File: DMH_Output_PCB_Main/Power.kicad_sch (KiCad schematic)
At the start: 79 parts, among them J0 Conn_01x01, J10 Conn_01x06, J100 IDC_02x05, J23 Conn_01x06, U1 TL072, U10 NE5532, U11 TL074, U12 NE5532, U13 NE5532, U14 NE5532, U15 NE5532, U16 NE5532, U17 NE5532, U18 NE5532, U19 NE5532, U2 LM339, U20 TL072, U21 LM4040LP-10, U24 LM339, U25 LM339, U3 LM339, U4 LM339, U5 LM339, U6 LM339, U7 TL072, U8 TL074, U9 NE5532

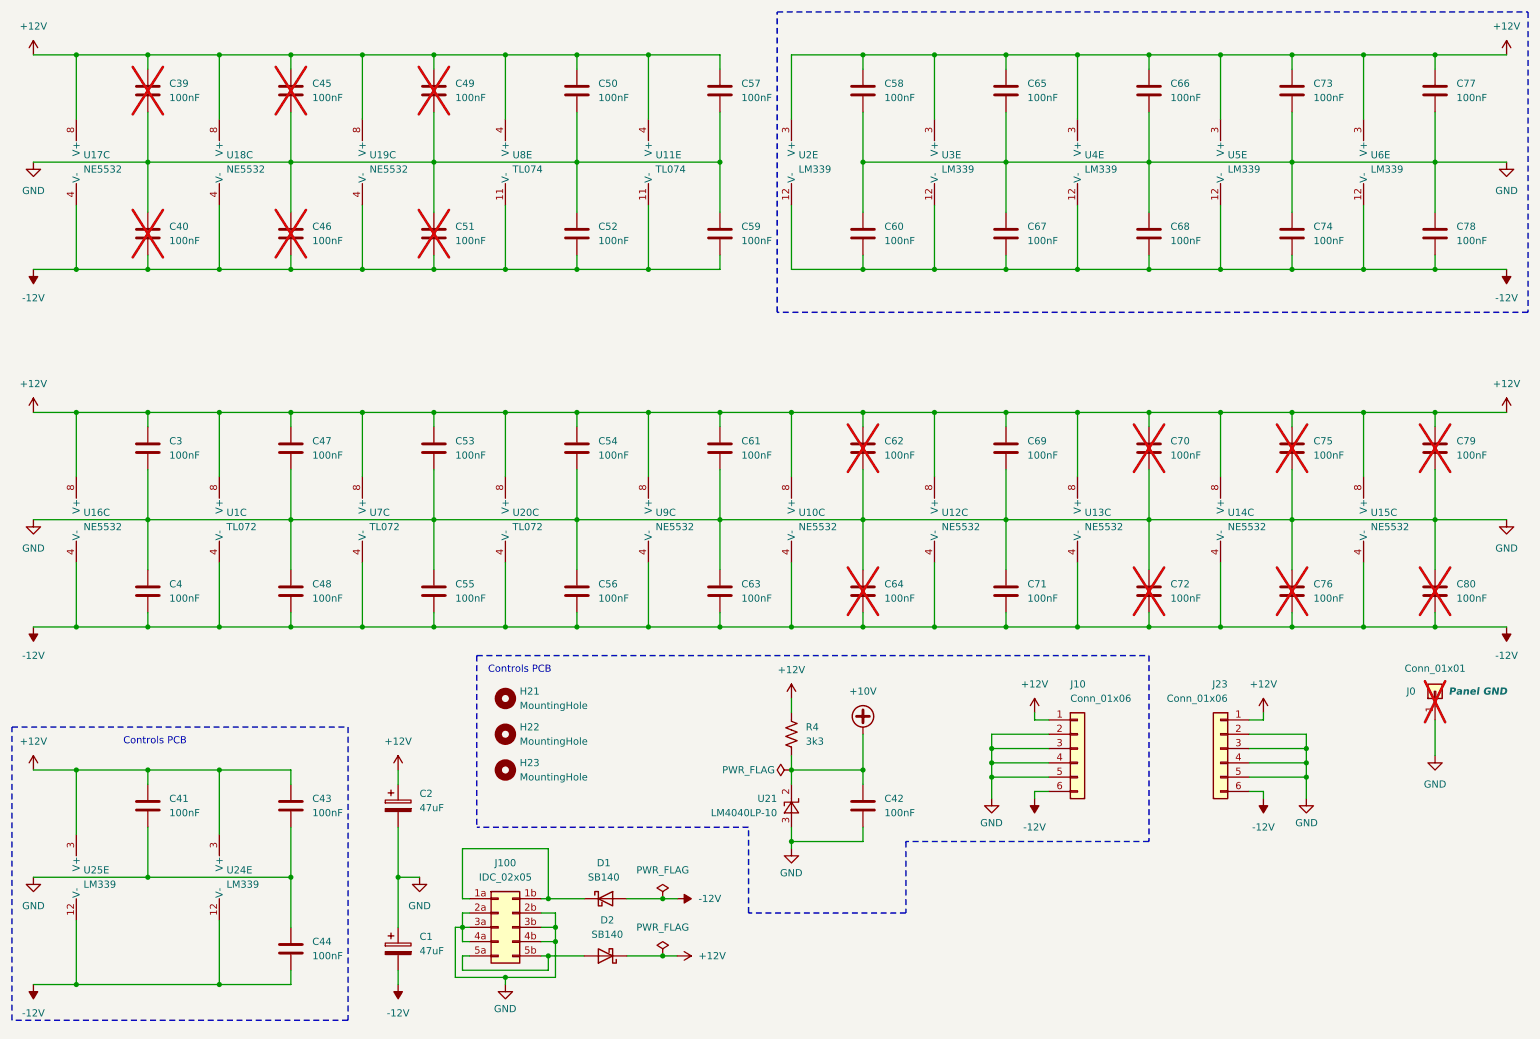
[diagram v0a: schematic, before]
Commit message: Preparing for split in submodules
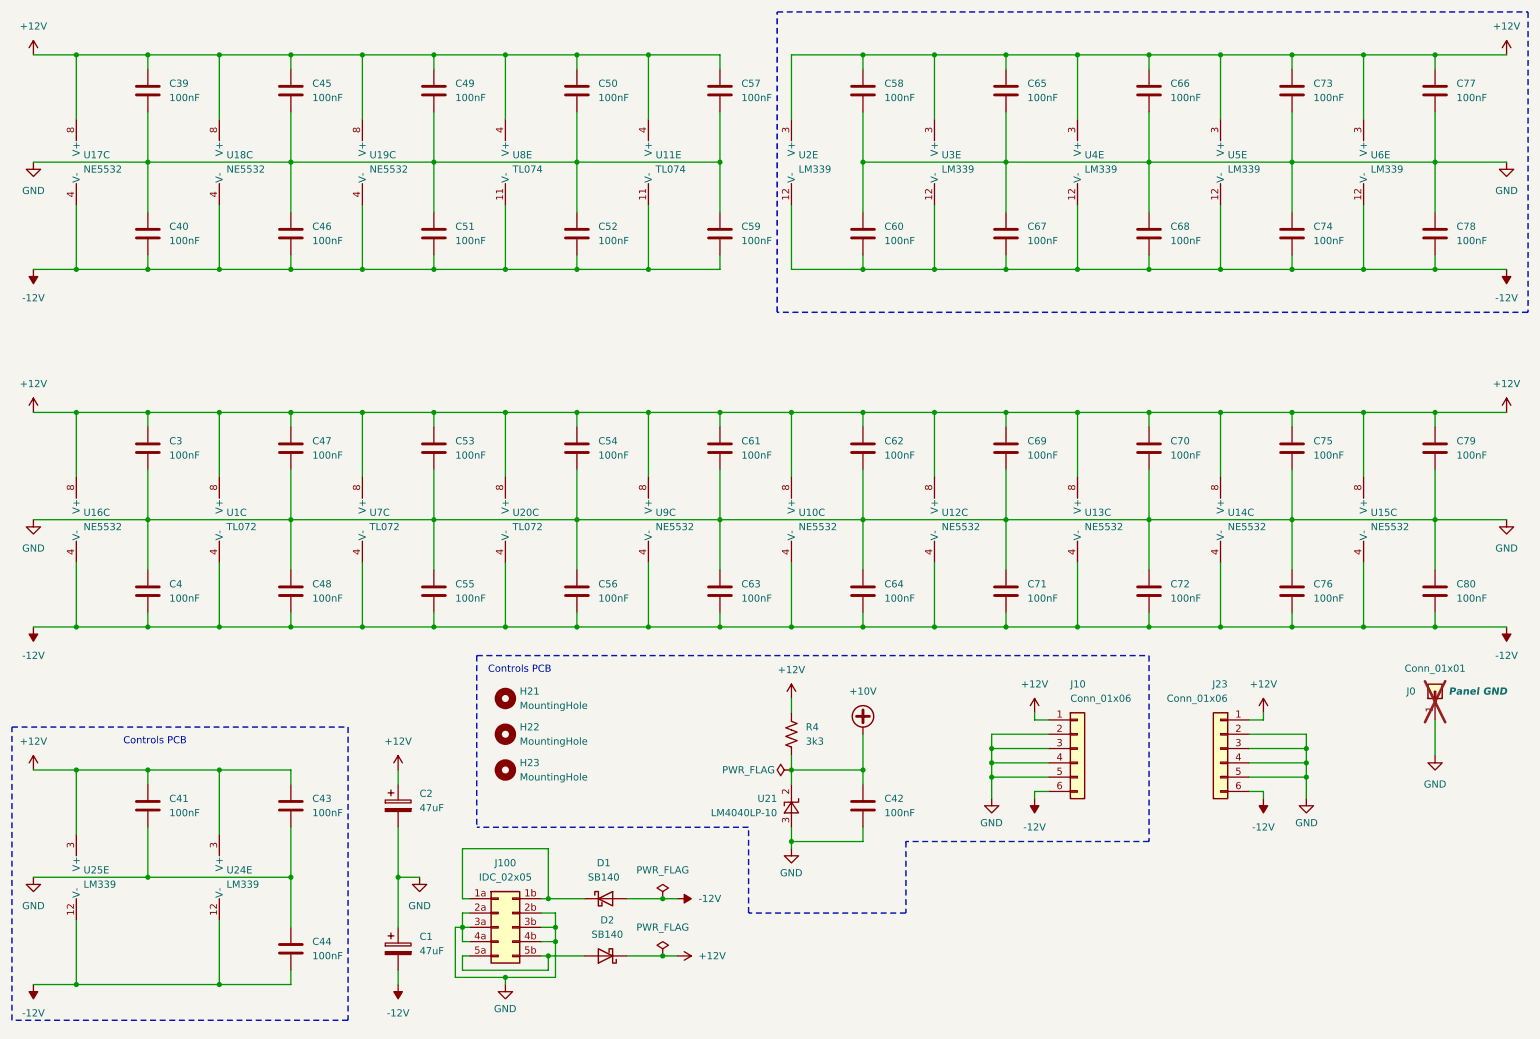
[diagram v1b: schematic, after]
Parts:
- C39, C40, C45, C46, C49, C51, C62, C64, C70, C72, C75, C76, C79, C80: now fitted; now in the parts list
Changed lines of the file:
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@@
 		(unit 1)
 		(exclude_from_sim no)
-		(in_bom no)
-		(on_board no)
-		(dnp yes)
+		(in_bom yes)
+		(on_board yes)
+		(dnp no)
 		(fields_autoplaced yes)
 		(property "Reference" "C76"
@@
 		(unit 1)
 		(exclude_from_sim no)
-		(in_bom no)
-		(on_board no)
-		(dnp yes)
+		(in_bom yes)
+		(on_board yes)
+		(dnp no)
 		(fields_autoplaced yes)
 		(property "Reference" "C75"
@@
 		(unit 1)
 		(exclude_from_sim no)
-		(in_bom no)
-		(on_board no)
-		(dnp yes)
+		(in_bom yes)
+		(on_board yes)
+		(dnp no)
 		(fields_autoplaced yes)
 		(property "Reference" "C64"
@@
 		(unit 1)
 		(exclude_from_sim no)
-		(in_bom no)
-		(on_board no)
-		(dnp yes)
+		(in_bom yes)
+		(on_board yes)
+		(dnp no)
 		(fields_autoplaced yes)
 		(property "Reference" "C70"
@@
 		(unit 1)
 		(exclude_from_sim no)
-		(in_bom no)
-		(on_board no)
-		(dnp yes)
+		(in_bom yes)
+		(on_board yes)
+		(dnp no)
 		(fields_autoplaced yes)
 		(property "Reference" "C62"
@@
 		(unit 1)
 		(exclude_from_sim no)
-		(in_bom no)
-		(on_board no)
-		(dnp yes)
+		(in_bom yes)
+		(on_board yes)
+		(dnp no)
 		(fields_autoplaced yes)
 		(property "Reference" "C46"
@@
 		(unit 1)
 		(exclude_from_sim no)
-		(in_bom no)
-		(on_board no)
-		(dnp yes)
+		(in_bom yes)
+		(on_board yes)
+		(dnp no)
 		(fields_autoplaced yes)
 		(property "Reference" "C51"
@@
 		(unit 1)
 		(exclude_from_sim no)
-		(in_bom no)
-		(on_board no)
-		(dnp yes)
+		(in_bom yes)
+		(on_board yes)
+		(dnp no)
 		(fields_autoplaced yes)
 		(property "Reference" "C40"
@@
 		(unit 1)
 		(exclude_from_sim no)
-		(in_bom no)
-		(on_board no)
-		(dnp yes)
+		(in_bom yes)
+		(on_board yes)
+		(dnp no)
 		(fields_autoplaced yes)
 		(property "Reference" "C72"
@@
 		(unit 1)
 		(exclude_from_sim no)
-		(in_bom no)
-		(on_board no)
-		(dnp yes)
+		(in_bom yes)
+		(on_board yes)
+		(dnp no)
 		(fields_autoplaced yes)
 		(property "Reference" "C49"
@@
 		(unit 1)
 		(exclude_from_sim no)
-		(in_bom no)
-		(on_board no)
-		(dnp yes)
+		(in_bom yes)
+		(on_board yes)
+		(dnp no)
 		(fields_autoplaced yes)
 		(property "Reference" "C80"
@@
 		(unit 1)
 		(exclude_from_sim no)
-		(in_bom no)
-		(on_board no)
-		(dnp yes)
+		(in_bom yes)
+		(on_board yes)
+		(dnp no)
 		(fields_autoplaced yes)
 		(property "Reference" "C79"
@@
 		(unit 1)
 		(exclude_from_sim no)
-		(in_bom no)
-		(on_board no)
-		(dnp yes)
+		(in_bom yes)
+		(on_board yes)
+		(dnp no)
 		(fields_autoplaced yes)
 		(property "Reference" "C39"
@@
 		(unit 1)
 		(exclude_from_sim no)
-		(in_bom no)
-		(on_board no)
-		(dnp yes)
+		(in_bom yes)
+		(on_board yes)
+		(dnp no)
 		(fields_autoplaced yes)
 		(property "Reference" "C45"

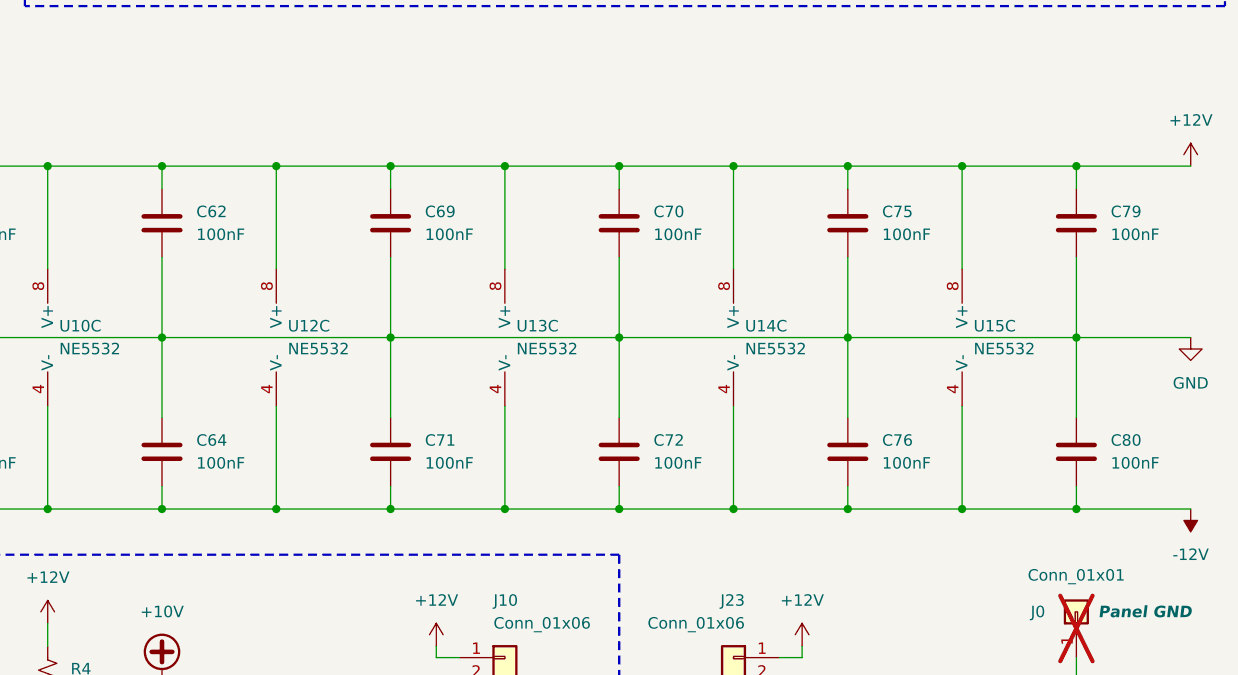
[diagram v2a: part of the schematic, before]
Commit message: Replaced jack symbols with 5pin ones
Also updated Meter LED current source resistor to 75R
Also increased LED guiding PCB mounting holes to M2.5
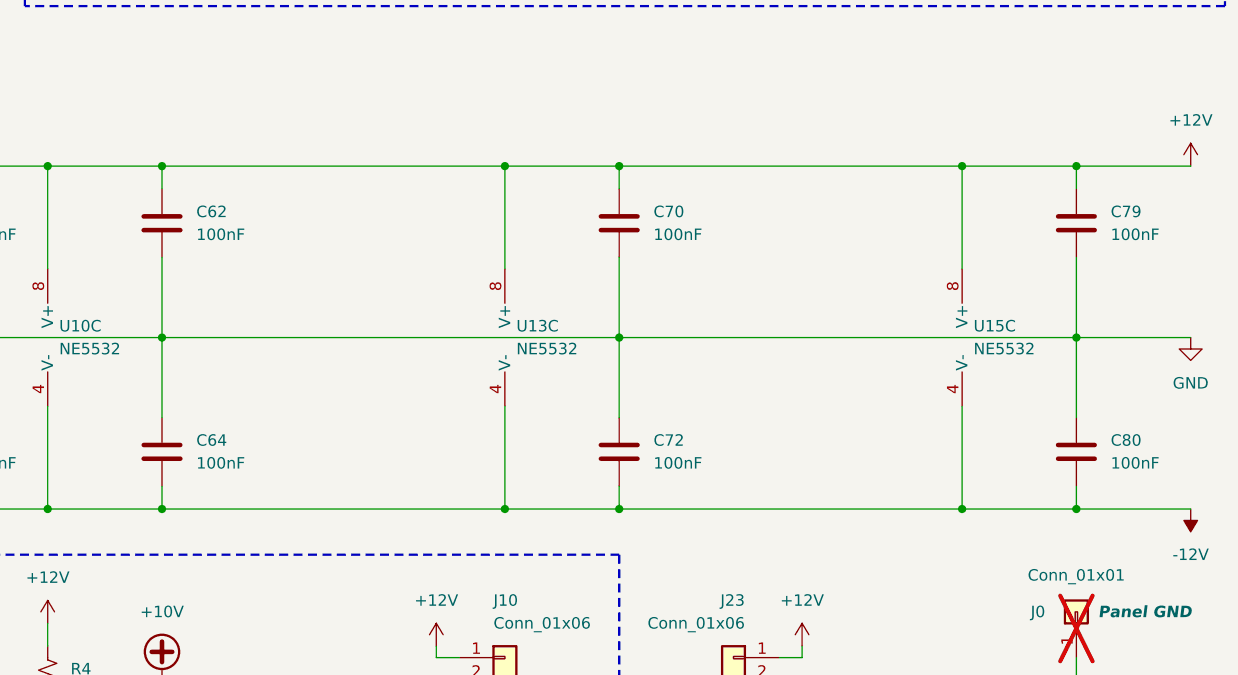
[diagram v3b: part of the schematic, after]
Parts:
- removed C69, C71, C75, C76: 100nF, Capacitor_THT:C_Disc_D4.3mm_W1.9mm_P5.00mm, symbol Device:C
- removed U12, U14: NE5532, Package_DIP:DIP-8_W7.62mm_Socket, symbol Amplifier_Operational:NE5532

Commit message: Prepped for Main PCB design
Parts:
- removed H23: MountingHole, MountingHole:MountingHole_2.2mm_M2, symbol Mechanical:MountingHole
- added J34: Conn_01x06, Connector_PinHeader_2.54mm:PinHeader_1x06_P2.54mm_Vertical, symbol Connector_Generic:Conn_01x06
- J23: footprint Connector_PinHeader_2.54mm:PinHeader_1x06_P2.54mm_Vertical -> Connector_PinSocket_2.54mm:PinSocket_1x06_P2.54mm_Vertical
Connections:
- net +12V: now also J34.1 (Pin_1)
- net -12V: now also J34.6 (Pin_6)
- net GND: now also J34.2 (Pin_2), J34.3 (Pin_3), J34.4 (Pin_4), J34.5 (Pin_5)
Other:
- note added: "Mezanine PCB"
- moved on the sheet: J0, J23
